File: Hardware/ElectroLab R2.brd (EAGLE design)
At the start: 175 x 100 mm, 241 parts, among them IC1 LM2902DT, IC10 CD4511BNSR, IC11 PAM8403, IC12 LM2902DT, IC2 LM2902DT, IC3 SN74LV08ADR, IC4 SN74LV32ADR, IC5 SN74LV04ADR, IC6 4027D, IC7 4027D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

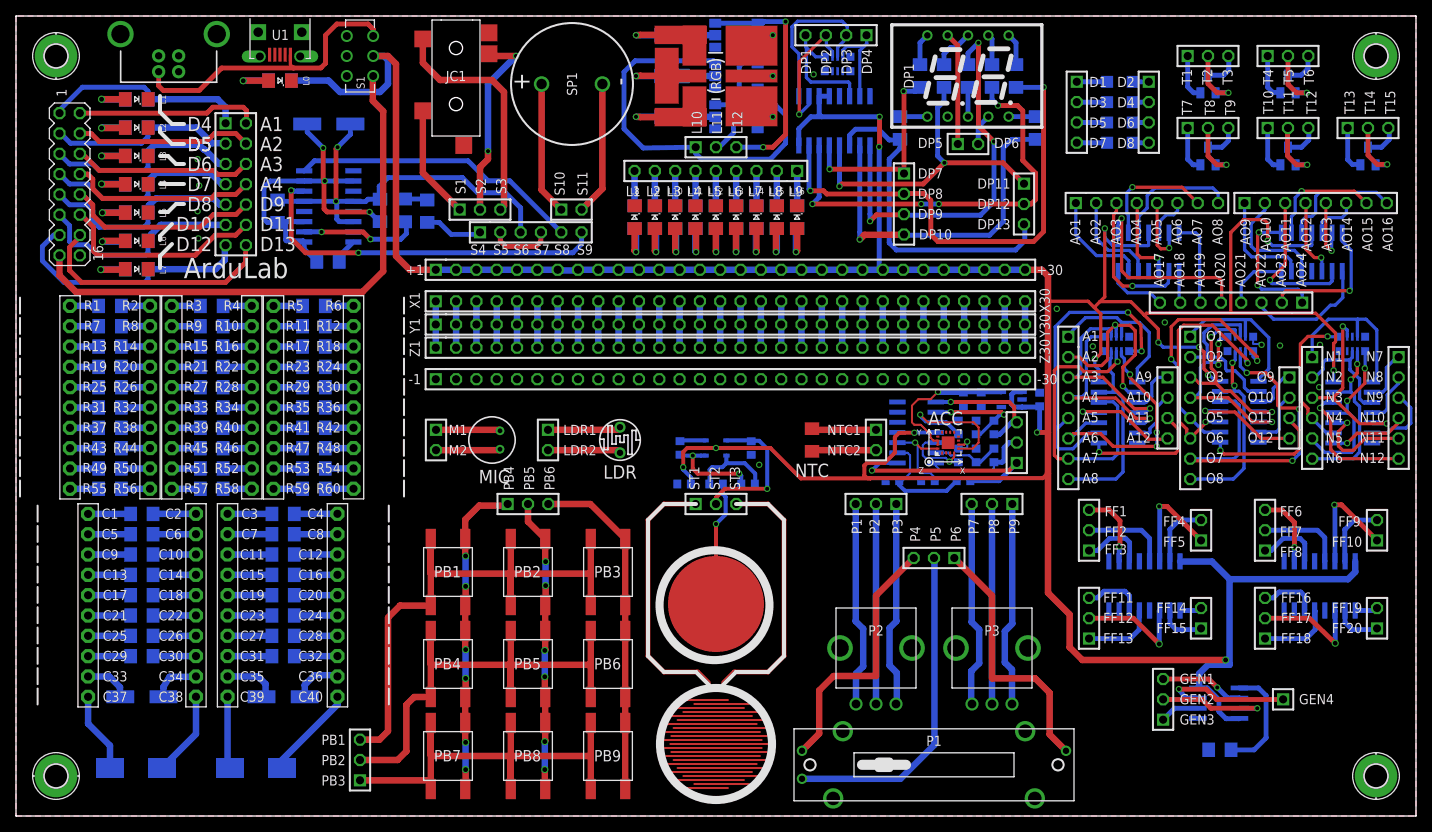
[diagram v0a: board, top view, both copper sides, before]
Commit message: Upgraded Electrolitic Capacitors to Tantalum Capacitors (C15-C18, C27)
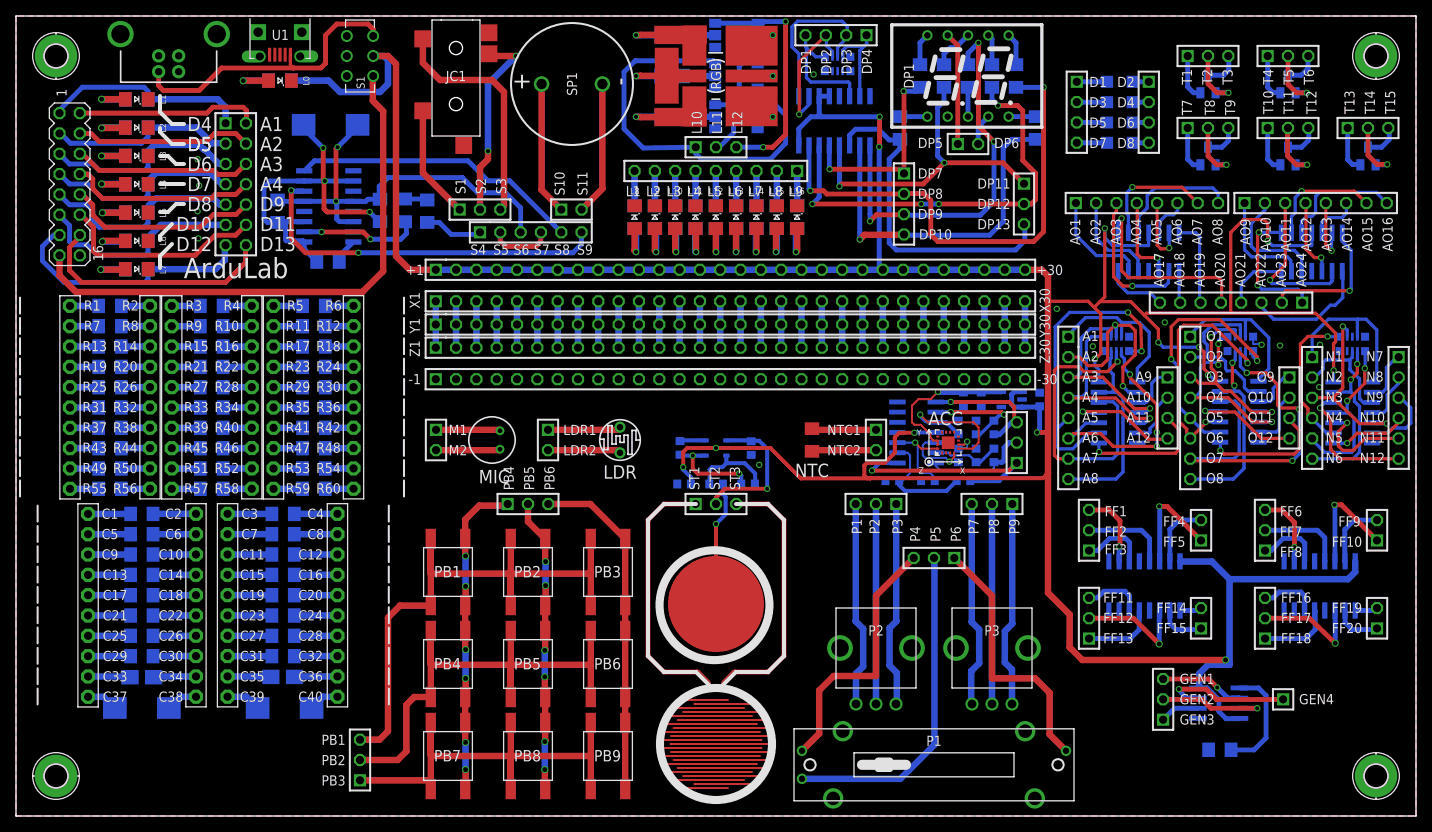
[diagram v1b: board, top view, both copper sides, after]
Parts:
- C17, C18: device resistor:153CLV-0605 -> rcl:A/3216-18W
- C19, C20: device resistor:153CLV-0810 -> rcl:D/7343-31W
- C27: device resistor:153CLV-0605 -> rcl:D/7343-31W
- moved C19 8.31 mm to (33.6, 13.5)
- moved C20 7.53 mm to (15.7, 13.5)
- moved C17 2.49 mm to (33.3, 17.4)
- moved C18 2.45 mm to (15.7, 17.4)
- moved C27 0.25 mm to (39.3, 86.4)
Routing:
- net N$80: track 11.8 -> 3.81 mm
- net N$91: track 10.7 -> 3.98 mm
- net N$90: track 10.0 -> 3.92 mm
- net N$70: track 9.04 -> 4.34 mm
- net N$69: track 7.25 -> 5.45 mm
- net N$79: track 6.14 -> 5.39 mm
- net N$92: track 6.03 -> 5.34 mm

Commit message: Jumpers added to accelerometer outputs to optionally get the raw signal
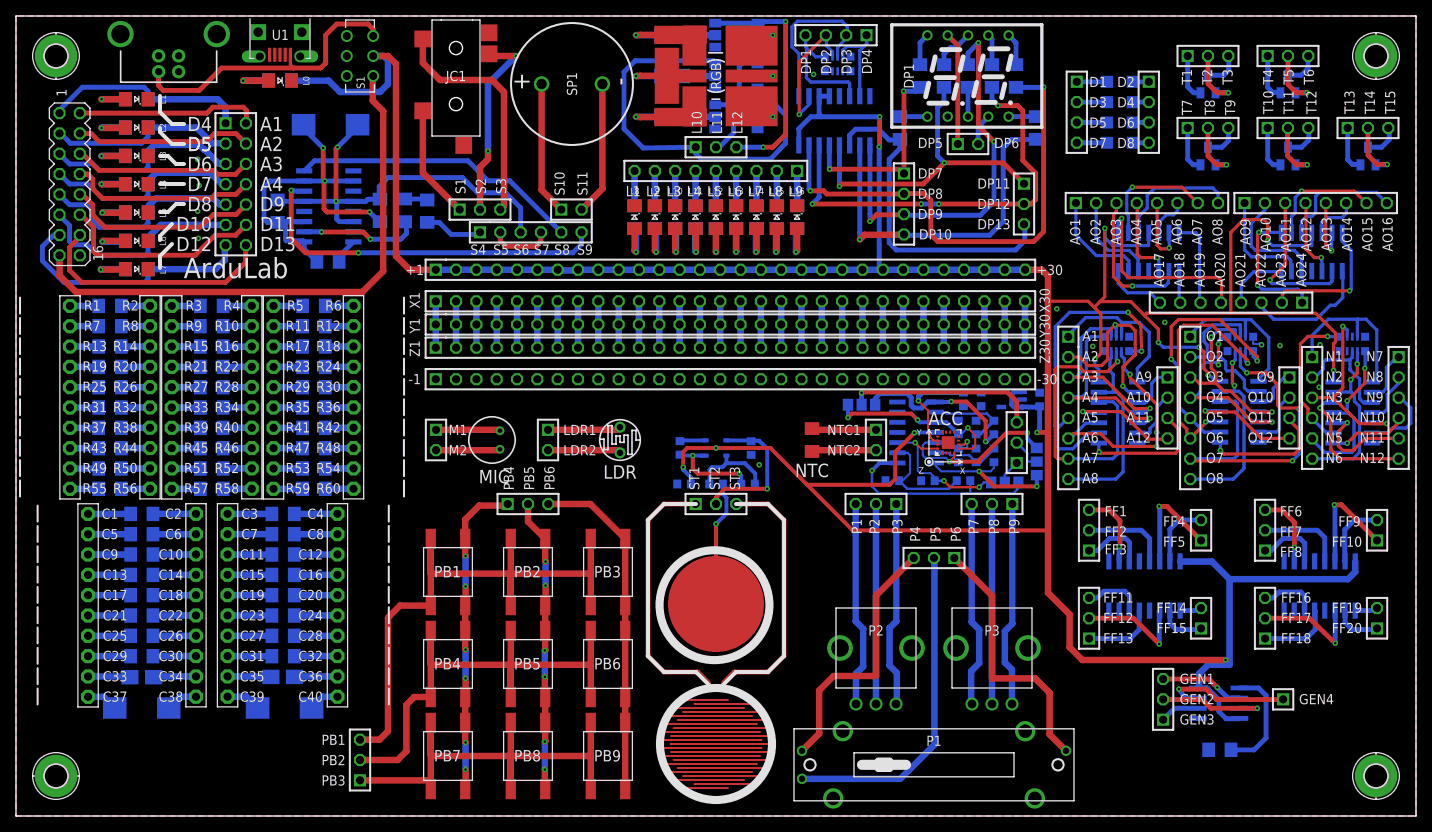
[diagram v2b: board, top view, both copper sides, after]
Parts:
- added JMP7, JMP8, JMP9: 0R-JUMPA, jump-0r-smd:A0R-JMP
- PH30: device pinhead:1X04 -> pinhead:1X03
- PH35: device pinhead:1X03 -> pinhead:1X04
- R62: value 2k -> 1k
- R65: value 1k -> 2k
- moved PH30 55.7 mm to (125.1, 46.7), turned to 90 degrees
- moved PH35 55.7 mm to (102.5, 97.6), turned to 180 degrees
- moved R63 4.96 mm to (118.4, 41.9), turned to 0 degrees
- moved R62 4.14 mm to (122.2, 45.1)
- moved R65 3.55 mm to (120.0, 45.1), turned to 90 degrees
- moved R64 3.49 mm to (120.0, 48.6)
- renumbered ACC to IC13, SV1 to PH63, U4 to IC14
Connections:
- new net N$124: JMP8.2, PH30.2
- new net N$127: JMP7.2, PH30.3
- new net N$128: JMP9.2, PH30.1
- net GND: now also R65.2; no longer R62.2
- net IA: now also PH35.1; no longer PH30.1
- net IB: now also PH35.2; no longer PH30.2
- net IC: now also PH35.3; no longer PH30.3
- net ID: now also PH35.4; no longer PH30.4
- net X: now also JMP7.3; no longer PH35.3
- net X+: now also JMP7.1
- net X-: now also R64.1; no longer R62.1
- net Y: now also JMP8.3, R62.1; no longer PH35.2, R63.1
- net Y+: now also JMP8.1
- net Y-: now also R62.2, R65.1; no longer R63.2, R64.1
- net Z: now also JMP9.3, R63.1; no longer PH35.1, R65.1
- net Z+: now also JMP9.1
- net Z-: now also R63.2; no longer R65.2
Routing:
- net N$127: track 0.00 -> 24.0 mm, vias 0 -> 1
- net Y+: track 9.66 -> 23.4 mm, vias 1 -> 2
- net VCC: track 473.5 -> 482.8 mm
- net Z+: track 11.9 -> 19.5 mm, vias 1 -> 3
- net 3.3V: track 25.4 -> 18.2 mm
- net X: track 15.6 -> 21.5 mm, vias 1 -> 2
- net Y: track 13.5 -> 18.2 mm, vias 0 -> 2
- net X+: track 18.6 -> 23.1 mm, vias 1 -> 3
- net N$124: track 0.00 -> 4.11 mm
- net N$128: track 0.00 -> 3.05 mm
- net X-: track 13.2 -> 10.6 mm, vias 2 -> 0
- net Z: track 28.8 -> 26.9 mm
- net Z-: track 14.3 -> 13.7 mm

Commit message: Replaced Microphone footprint to fit with CMEJ-0627-42-P
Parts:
- MIC: value (none) -> ELECTRET_MICROPHON-WM-64PC/64PK
- moved MIC 0.10 mm to (59.4, 47.0)
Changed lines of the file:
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@@
 <attribute name="NAME" x="122" y="39" size="1.27" layer="49" rot="R180" align="center"/>
 </element>
-<element name="MIC" library="microphon" package="WM-64PC/64PK" value="" x="59.5" y="47" smashed="yes" rot="R180">
-<attribute name="NAME" x="59.754" y="42.428" size="1.6764" layer="25" rot="R180" align="center"/>
-<attribute name="VALUE" x="59.754" y="51.572" size="1.27" layer="27" rot="R180" align="center"/>
+<element name="MIC" library="microphon" package="WM-64PC/64PK" package3d_urn="urn:adsk.eagle:package:21034/1" value="ELECTRET_MICROPHON-WM-64PC/64PK" x="59.4" y="47" smashed="yes" rot="R180">
+<attribute name="NAME" x="59.654" y="42.428" size="1.6764" layer="25" rot="R180" align="center"/>
+<attribute name="VALUE" x="59.654" y="51.572" size="1.27" layer="27" rot="R180" align="center"/>
 </element>
 <element name="PH4" library="pinhead" package="1X02" value="" x="52.5" y="47" smashed="yes" rot="R270">
@@
 <contactref element="MIC" pad="2"/>
 <contactref element="PH4" pad="1"/>
-<wire x1="52.5" y1="48.27" x2="60.38" y2="48.27" width="0.8128" layer="1"/>
-<wire x1="60.38" y1="48.27" x2="60.5" y2="48.15" width="0.8128" layer="1"/>
+<wire x1="52.5" y1="48.27" x2="59.93" y2="48.27" width="0.6096" layer="16"/>
+<wire x1="59.93" y1="48.27" x2="60.4" y2="47.8" width="0.6096" layer="16"/>
 </signal>
 <signal name="N$250">
 <contactref element="MIC" pad="1"/>
 <contactref element="PH4" pad="2"/>
-<wire x1="52.5" y1="45.73" x2="60.38" y2="45.73" width="0.8128" layer="1"/>
-<wire x1="60.38" y1="45.73" x2="60.5" y2="45.85" width="0.8128" layer="1"/>
+<wire x1="52.5" y1="45.73" x2="59.93" y2="45.73" width="0.6096" layer="16"/>
+<wire x1="59.93" y1="45.73" x2="60.4" y2="46.2" width="0.6096" layer="16"/>
 </signal>
 <signal name="SNSK">
